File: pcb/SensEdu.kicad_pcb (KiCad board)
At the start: 4 copper layers, 99.1 x 54 mm, 147 parts, among them J1 Power, J10 Barrel_Jack_Switch, J11 Conn_01x04_Pin, J12 Conn_01x04_Pin, J13 Conn_02x01, J14 Conn_02x01, J15 Conn_02x01, J16 Conn_02x01, J19 Conn_03x01, J2 PWM, J20 Conn_01x04_Pin, J3 Analog, J4 PWM, J5 Analog, J6 Communication, J7 Digital, J9 Conn_01x04_Pin, U1 AD8426ACPZ-R7, U12 TLS850C2TE_V33, U13 NCP1117-2.5_SOT223, U2 AD8426ACPZ-R7, U3 LT1790ACS6-1.25, U4 ADA4891, U5 AD8426ACPZ-R7, U6 AD8426ACPZ-R7, U7 ADA4891, U8 DPS310XTSA1

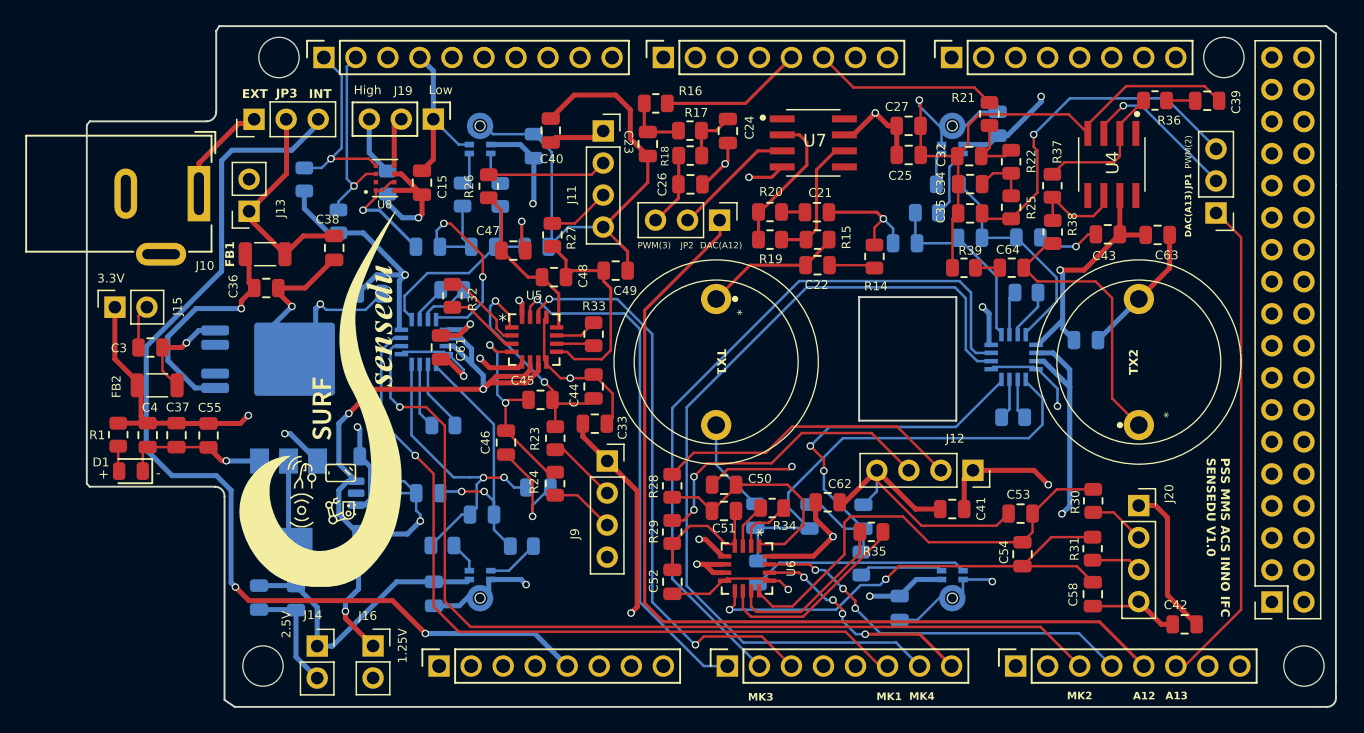
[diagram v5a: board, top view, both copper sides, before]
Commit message: Progress in pcb routing
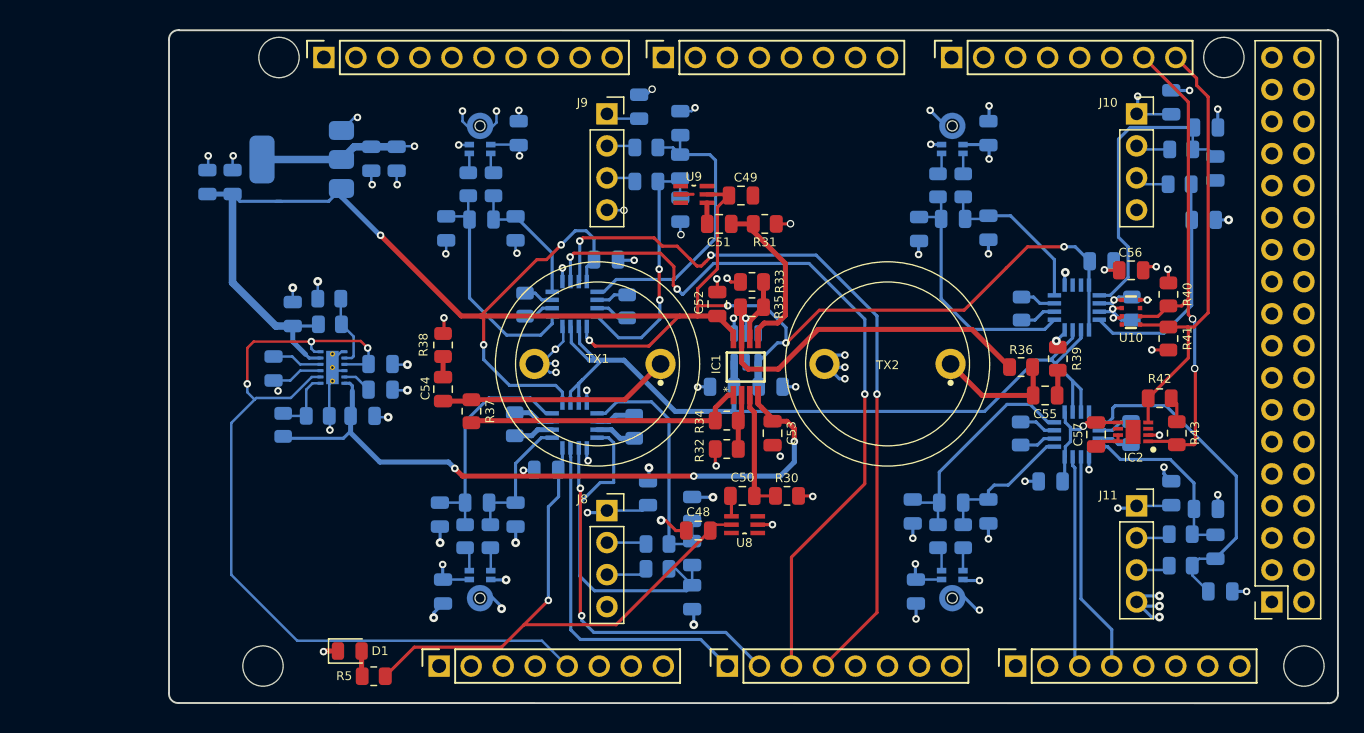
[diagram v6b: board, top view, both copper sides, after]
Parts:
- removed C58: 100p, Capacitor_SMD:C_0805_2012Metric
- removed C61, C62: 1u, Capacitor_SMD:C_0805_2012Metric
- removed C63: 100n, Capacitor_SMD:C_0805_2012Metric
- removed C64: DNI, Capacitor_SMD:C_0805_2012Metric
- removed FB1, FB2: FerriteBead, Inductor_SMD:L_1206_3216Metric
- removed G***: LOGO, wave colour:logo2
- removed the J10 at (108.9, 60.0)
- removed J13, J14, J15, J16: Conn_02x01, Connector_PinSocket_2.54mm:PinSocket_1x02_P2.54mm_Vertical
- removed J19: Conn_03x01, Connector_PinHeader_2.54mm:PinHeader_1x03_P2.54mm_Vertical
- removed JP1, JP2, JP3: Jumper_3_Bridged12, Connector_PinHeader_2.54mm:PinHeader_1x03_P2.54mm_Vertical
- removed LS1, LS2: 328ST16M, SensEdu:328ST16M_Speaker
- removed U12: TLS850C2TE_V33, Package_TO_SOT_SMD:TO-252-4
- removed U13: NCP1117-2.5_SOT223, Package_TO_SOT_SMD:SOT-223-3_TabPin2
- added C19: 100p, Capacitor_SMD:C_0805_2012Metric, B.Cu at (165.5, 85.2)
- added IC1: ADA4511-2ARMZ, SensEdu:ADA4511, F.Cu at (152.2, 73.8)
- added IC2: SHT35-DIS-B2.5KS, SensEdu:SHT35-DIS-B2.5KS, F.Cu at (183.0, 78.9)
- added R43: 10k, Resistor_SMD:R_0805_2012Metric, F.Cu at (186.4, 79.0)
- added TX1: 328ST16M, SensEdu:328ST16M_Speaker, F.Cu at (140.5, 73.5)
- added TX2: 328ST16M, SensEdu:328ST16M_Speaker, F.Cu at (163.5, 73.5)
- added U10: DPS368XTSA1, SensEdu:DPS368XTSA1, F.Cu at (182.8, 69.4)
- added U9: NC7SB3157P6X, SensEdu:SOT65P210X110-6N, F.Cu at (148.1, 60.1)
- C1: value 100n -> 4.7u
- C11: value 100n -> 1u
- C12: value 470p -> 1u
- C13, C17: value 470p -> 100p
- C14: value 1u -> 470p
- C15, C25, C39, C44, C45, C46, R24, R26, R27, R28, R29, U5, U6: moved to B.Cu
- C18: value 100p -> 470p
- C2: value 100n -> 470n
- C20, C7: value 1u -> 100n
- C21, C36: value 100n -> 1u; moved to B.Cu
- C22: value DNI -> 100p; moved to B.Cu
- C23, C35: value 1n -> 100p; moved to B.Cu
- C24, C34: value 1n -> 100n; moved to B.Cu
- C26, C32: value 1n -> 470p; moved to B.Cu
- C27: value 1u -> 470p; moved to B.Cu
- C3: value 10u -> 2.2u; moved to B.Cu
- C31: value 100p -> 1u
- C33, C40, C42: value 100n -> 100p; moved to B.Cu
- C37: value 10u -> 470p; moved to B.Cu
- C38: value 10u -> 100p; moved to B.Cu
- C4: value 100n -> 2.2u; moved to B.Cu
- C41: value 100n -> 470p; moved to B.Cu
- C43: value 1u -> 100n; moved to B.Cu
- C47: value 100p -> 100n; moved to B.Cu
- C48: value 470p -> 10n
- C49: value 100p -> 10n
- C5: value 100p -> 4.7u
- C50: value 100p -> 2.2u
- C51: value 470p -> 2.2u
- C52, C53: value 100p -> 100n
- C54: value 470p -> DNI
- C55: value 100n -> DNI
- C56: value 10u -> 100n; moved to F.Cu
- C57, R42: moved to F.Cu
- C6: value 470p -> 10u
- C9: value 100p -> 10u
- R1: value 47 -> 130k; moved to B.Cu
- R11, R6: value 3.9k -> 1k
- R13, R7: value 1k -> 3.9k
- R14: value DNI -> 3.9k; moved to B.Cu
- R15: value 0 -> 3.9k; moved to B.Cu
- R16, R22: value 4.7k -> 3.9k; moved to B.Cu
- R17, R18, R21, R25: value 4.7k -> 1k; moved to B.Cu
- R19: value 3k -> 3.9k; moved to B.Cu
- R2: value 1k -> 75k
- R20: value 1k -> 3.9k; moved to B.Cu
- R23: value 3.9k -> 1k; moved to B.Cu
- R3: value 3.9k -> 130k
- R30, R31: value 3.9k -> 22k
- R32, R33, R34, R35: value 1k -> 22k
- R36: value 1k -> 0
- R37: value 3k -> 0
- R38: value 0 -> DNI
- R4: value 3.9k -> 75k
- R40, R41: value 10k -> 5k6; moved to F.Cu
- R5: value 3.9k -> 47; moved to F.Cu
- U1: value AD8426ACPZ-R7 -> LM27762DSST; footprint SensEdu:QFN65P400X400X100-16N -> SensEdu:IC_LM27762DSST
- U2: value AD8426ACPZ-R7 -> NCP1117-2.5_SOT223; footprint SensEdu:QFN65P400X400X100-16N -> Package_TO_SOT_SMD:SOT-223-3_TabPin2
- U4, U7: value ADA4891 -> AD8426ACPZ-R7; footprint SensEdu:ADA4891-1ARZ -> SensEdu:QFN65P400X400X100-16N; moved to B.Cu
- U8: value DPS310XTSA1 -> NC7SB3157P6X; footprint SensEdu:XDCR_DPS310XTSA1 -> SensEdu:SOT65P210X110-6N
- moved C56 71.2 mm to (182.8, 66.1), turned to 0 degrees
- moved R40 69.1 mm to (185.8, 68.0)
- moved C57 67.6 mm to (180.0, 79.1), turned to 90 degrees
- moved R41 66.5 mm to (185.8, 71.5), turned to -90 degrees
- moved C55 66.4 mm to (176.0, 76.0), turned to 0 degrees
- moved C36 64.1 mm to (176.4, 82.8), turned to 180 degrees
- moved R42 63.6 mm to (185.1, 76.2), turned to 180 degrees
- moved C6 58.6 mm to (111.6, 59.1), turned to 90 degrees
- moved U2 58.6 mm to (117.0, 57.3), turned to 180 degrees
- moved C46 55.8 mm to (188.8, 85.0), turned to 180 degrees
- moved C47 55.6 mm to (186.0, 83.8), turned to 90 degrees
- moved R26 54.8 mm to (186.7, 59.2), turned to 0 degrees
- moved C45 54.8 mm to (189.5, 88.0), turned to -90 degrees
- moved C2 53.2 mm to (114.8, 73.9)
- moved C1 52.5 mm to (123.3, 73.5), turned to 0 degrees
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- renumbered J3 to J1, J12 to J10, J20 to J11, J5 to J2, J1 to J3, J7 to J4, J2 to J5, J4 to J6, J6 to J7, J9 to J8, J11 to J9, MK4 to MK2, MK2 to MK3, MK3 to MK4
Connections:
- net /48 renamed SE_PWM_3
- C1 pad 1: +2.5V -> /+5V_ARDUINO
- C11 pad 1: +2.5V -> GND
- C11 pad 2: GND -> +1.25V_REF
- C12 pad 1: /Microphones/mic2_out1 -> +3.3V
- C12 pad 2: /Microphones/mic2_out2 -> GND
- C13 pad 1: /Microphones/mic1_out1 -> GND
- C13 pad 2: /Microphones/mic1_out2 -> mic1_out2
- C14 pad 1: +3.3V -> mic1_out1
- C14 pad 2: GND -> mic1_out2
- C15 pad 1: +3.3V -> +2.5V
- C16 pad 2: /Microphones/mic4_out1 -> mic2_out2
- C17 pad 1: /Microphones/mic4_out1 -> GND
- C17 pad 2: /Microphones/mic4_out2 -> mic1_out1
- C18 pad 1: GND -> mic2_out1
- C18 pad 2: /Microphones/mic4_out2 -> mic2_out2
- C2 pad 1: +2.5V -> Net-(U1-C1+)
- C2 pad 2: GND -> Net-(U1-C1-)
- C20 pad 1: +3.3V -> +2.5V
- C21 pad 1: Net-(C21-Pad1) -> +3.3V
- C22 pad 1: Net-(C22-Pad1) -> GND
- C22 pad 2: Net-(C22-Pad2) -> mic4_out2
- C23 pad 1: Net-(C23-Pad1) -> GND
- C23 pad 2: GND -> mic3_out2
- C24 pad 1: Net-(C24-Pad1) -> +2.5V
- C25 pad 1: GND -> +2.5V
- C25 pad 2: +3.3V -> GND
- C26 pad 1: Net-(JP2-B) -> mic3_out1
- C26 pad 2: GND -> mic3_out2
- C27 pad 1: GND -> mic4_out1
- C27 pad 2: +3.3V -> mic4_out2
- C28 pad 2: /Microphones/mic2_out1 -> mic3_out1
- C29 pad 2: /Microphones/mic2_out2 -> mic4_out1
- C3 pad 1: Net-(U12-Q) -> +3.3V
- C30 pad 2: /Microphones/mic1_out1 -> mic5_out2
- C31 pad 1: GND -> +3.3V
- C31 pad 2: /Microphones/mic1_out2 -> GND
- C32 pad 1: Net-(C32-Pad1) -> mic5_out1
- C32 pad 2: GND -> mic5_out2
- C33 pad 1: +2.5V -> GND
- C33 pad 2: GND -> mic5_out1
- C34 pad 1: Net-(C34-Pad1) -> +2.5V
- C35 pad 1: Net-(JP1-B) -> GND
- C35 pad 2: GND -> mic6_out2
- C36 pad 1: Net-(U12-I) -> +3.3V
- C37 pad 1: +3.3V -> mic6_out1
- C37 pad 2: GND -> mic6_out2
- C38 pad 1: Net-(J13-Pin_1) -> GND
- C38 pad 2: GND -> mic6_out1
- C39 pad 1: Net-(C39-Pad1) -> +2.5V
- C4 pad 1: +3.3V -> GND
- C4 pad 2: GND -> -3V3
- C40 pad 1: +2.5V -> GND
- C40 pad 2: GND -> mic7_out2
- C41 pad 1: +2.5V -> mic7_out1
- C41 pad 2: GND -> mic7_out2
- C42 pad 1: +2.5V -> GND
- C42 pad 2: GND -> mic7_out1
- C43 pad 1: GND -> +2.5V
- C43 pad 2: +3.3V -> GND
- C44 pad 2: /Microphones/External Microphone Connectors/mic5_out1 -> mic8_out2
- C45 pad 1: /Microphones/External Microphone Connectors/mic5_out1 -> mic8_out1
- C45 pad 2: /Microphones/External Microphone Connectors/mic5_out2 -> mic8_out2
- C46 pad 2: /Microphones/External Microphone Connectors/mic5_out2 -> mic8_out1
- C47 pad 1: GND -> +2.5V
- C47 pad 2: /Microphones/External Microphone Connectors/mic6_out1 -> GND
- C48 pad 1: /Microphones/External Microphone Connectors/mic6_out1 -> GND
- C48 pad 2: /Microphones/External Microphone Connectors/mic6_out2 -> +3.3V
- C49 pad 2: /Microphones/External Microphone Connectors/mic6_out2 -> +3.3V
- C5 pad 1: GND -> /Power/CP
- C5 pad 2: /Microphones/mic3_out1 -> GND
- C50 pad 1: GND -> /Speakers/SW1_OUT
- C50 pad 2: /Microphones/External Microphone Connectors/mic7_out1 -> /Speakers/+IN_CH1
- C51 pad 1: /Microphones/External Microphone Connectors/mic7_out1 -> /Speakers/SW2_OUT
- C51 pad 2: /Microphones/External Microphone Connectors/mic7_out2 -> /Speakers/+IN_CH2
- C52 pad 1: GND -> +3.3V
- C52 pad 2: /Microphones/External Microphone Connectors/mic7_out2 -> GND
- C53 pad 2: /Microphones/External Microphone Connectors/mic8_out1 -> -3V3
- C54 pad 1: /Microphones/External Microphone Connectors/mic8_out1 -> /Speakers/TX1
- C54 pad 2: /Microphones/External Microphone Connectors/mic8_out2 -> Net-(C54-Pad2)
- C55 pad 1: +3.3V -> /Speakers/TX2
- C55 pad 2: GND -> Net-(C55-Pad2)
- C57 pad 1: +2.5V -> GND
- C57 pad 2: GND -> +3.3V
- C6 pad 1: /Microphones/mic3_out1 -> +3.3V
- C6 pad 2: /Microphones/mic3_out2 -> GND
- C7 pad 1: GND -> +3.3V
- C7 pad 2: +1.25V_REF -> GND
- C9 pad 1: GND -> +2.5V
- C9 pad 2: /Microphones/mic3_out2 -> GND
- D1 pad 2: Net-(D1-A) -> /Power/LED+
- J1 pad 1: /A0 -> /OUT_MIC5
- J1 pad 2: /A1 -> /OUT_MIC6
- J1 pad 3: /A2 -> /OUT_MIC2
- J1 pad 4: /A3 -> /OUT_MIC1
- J1 pad 6: /A5 -> unconnected-(J1-Pin_6-Pad6)
- J1 pad 7: /A6 -> unconnected-(J1-Pin_7-Pad7)
- J1 pad 8: /A7 -> unconnected-(J1-Pin_8-Pad8)
- J10 pad 2: Net-(J12-Pin_2) -> /Microphones/External Microphone Connectors/out+
- J10 pad 3: Net-(J12-Pin_3) -> /Microphones/External Microphone Connectors/out-
- J11 pad 2: Net-(J20-Pin_2) -> /Microphones/External Microphone Connectors/out+
- J11 pad 3: Net-(J20-Pin_3) -> /Microphones/External Microphone Connectors/out-
- J2 pad 1: /A8 -> /OUT_MIC3
- J2 pad 2: /A9 -> /OUT_MIC4
- J2 pad 3: /A10 -> /OUT_MIC7
- J2 pad 4: /Microphones/MIC7_OUT -> /OUT_MIC8
- J2 pad 5: A12 -> DAC0
- J2 pad 6: A13 -> DAC1
- J3 pad 5: /5V0 -> /+5V_ARDUINO
- J4 pad 20: /37 -> SE_PWM_2
- J6 pad 1: /*7 -> S1
- J6 pad 2: /*6 -> S2
- J6 pad 4: /*4 -> SE_PWM_1
- J6 pad 5: /*3 -> /4*
- J6 pad 6: /*2 -> /3*
- J7 pad 7: /SDA/20 -> /SDA
- J7 pad 8: /SCL/21 -> /SCL
- J8 pad 2: Net-(J9-Pin_2) -> /Microphones/External Microphone Connectors/out+
- J8 pad 3: Net-(J9-Pin_3) -> /Microphones/External Microphone Connectors/out-
- J9 pad 2: Net-(J11-Pin_2) -> /Microphones/External Microphone Connectors/out+
- J9 pad 3: Net-(J11-Pin_3) -> /Microphones/External Microphone Connectors/out-
- MK2 pad 3: Net-(MK4-OUTPUT-) -> Net-(MK2-OUTPUT-)
- MK3 pad 1: Net-(MK2-OUTPUT+) (its old number) -> Net-(MK3-OUTPUT+)
- MK3 pad 3: Net-(MK2-OUTPUT-) -> Net-(MK3-OUTPUT-)
- MK4 pad 1: Net-(MK3-OUTPUT+) -> Net-(MK4-OUTPUT+)
- MK4 pad 3: Net-(MK3-OUTPUT-) -> Net-(MK4-OUTPUT-)
- R1 pad 2: Net-(D1-A) -> /Power/FB+
- R10 pad 2: /Microphones/mic4_out1 -> mic2_out1
- R11 pad 1: Net-(MK4-OUTPUT-) -> Net-(U4-RG2_2)
- R11 pad 2: /Microphones/mic4_out2 -> Net-(U4-RG2)
- R12 pad 1: Net-(U2-RG1_2) -> Net-(U5-RG1_2)
- R12 pad 2: Net-(U2-RG1) -> Net-(U5-RG1)
- R13 pad 1: Net-(U2-RG2_2) -> Net-(MK4-OUTPUT-)
- R13 pad 2: Net-(U2-RG2) -> mic4_out2
- R14 pad 1: GND -> Net-(MK3-OUTPUT-)
- R14 pad 2: Net-(C22-Pad2) -> mic3_out2
- R15 pad 1: Net-(U7-OUT) -> Net-(MK3-OUTPUT+)
- R15 pad 2: Net-(C22-Pad1) -> mic3_out1
- R16 pad 1: Net-(C23-Pad1) -> Net-(MK4-OUTPUT+)
- R16 pad 2: /*3 -> mic4_out1
- R17 pad 1: Net-(C23-Pad1) -> Net-(U5-RG2_2)
- R17 pad 2: Net-(C24-Pad1) -> Net-(U5-RG2)
- R18 pad 1: Net-(C24-Pad1) -> Net-(U6-RG1_2)
- R18 pad 2: Net-(JP2-B) -> Net-(U6-RG1)
- R19 pad 1: Net-(U7--IN) -> /Microphones/External Microphone Connectors/out-
- R19 pad 2: Net-(U7-OUT) -> mic5_out2
- R2 pad 1: Net-(U1-RG1_2) -> /Power/FB+
- R2 pad 2: Net-(U1-RG1) -> GND
- R20 pad 1: Net-(U7--IN) -> /Microphones/External Microphone Connectors/out+
- R20 pad 2: Net-(C21-Pad1) -> mic5_out1
- R21 pad 1: Net-(C32-Pad1) -> Net-(U6-RG2_2)
- R21 pad 2: /*2 -> Net-(U6-RG2)
- R22 pad 1: Net-(C32-Pad1) -> /Microphones/External Microphone Connectors/out-
- R22 pad 2: Net-(C34-Pad1) -> mic6_out2
- R23 pad 1: Net-(J9-Pin_2) -> Net-(U7-RG1_2)
- R23 pad 2: /Microphones/External Microphone Connectors/mic5_out1 -> Net-(U7-RG1)
- R24 pad 1: Net-(J9-Pin_3) -> /Microphones/External Microphone Connectors/out+
- R24 pad 2: /Microphones/External Microphone Connectors/mic5_out2 -> mic6_out1
- R25 pad 1: Net-(C34-Pad1) -> Net-(U7-RG2_2)
- R25 pad 2: Net-(JP1-B) -> Net-(U7-RG2)
- R26 pad 1: Net-(J11-Pin_2) -> /Microphones/External Microphone Connectors/out-
- R26 pad 2: /Microphones/External Microphone Connectors/mic6_out1 -> mic7_out2
- R27 pad 1: Net-(J11-Pin_3) -> /Microphones/External Microphone Connectors/out+
- R27 pad 2: /Microphones/External Microphone Connectors/mic6_out2 -> mic7_out1
- R28 pad 1: Net-(J12-Pin_2) -> /Microphones/External Microphone Connectors/out-
- R28 pad 2: /Microphones/External Microphone Connectors/mic7_out1 -> mic8_out2
- R29 pad 1: Net-(J12-Pin_3) -> /Microphones/External Microphone Connectors/out+
- R29 pad 2: /Microphones/External Microphone Connectors/mic7_out2 -> mic8_out1
- R3 pad 1: Net-(MK2-OUTPUT+) (its old number) -> GND
- R3 pad 2: /Microphones/mic2_out1 -> /Power/FB-
- R30 pad 1: Net-(J20-Pin_2) -> GND
- R30 pad 2: /Microphones/External Microphone Connectors/mic8_out1 -> /Speakers/+IN_CH1
- R31 pad 1: Net-(J20-Pin_3) -> GND
- R31 pad 2: /Microphones/External Microphone Connectors/mic8_out2 -> /Speakers/+IN_CH2
- R32 pad 1: Net-(U5-RG1_2) -> GND
- R32 pad 2: Net-(U5-RG1) -> /Speakers/-IN_CH1
- R33 pad 1: Net-(U5-RG2_2) -> GND
- R33 pad 2: Net-(U5-RG2) -> /Speakers/-IN_CH2
- R34 pad 1: Net-(U6-RG1_2) -> /Speakers/-IN_CH1
- R34 pad 2: Net-(U6-RG1) -> /Speakers/TX1_IN
- R35 pad 1: Net-(U6-RG2_2) -> /Speakers/-IN_CH2
- R35 pad 2: Net-(U6-RG2) -> /Speakers/TX2_IN
- R36 pad 1: Net-(U4--IN) -> /Speakers/TX2_IN
- R36 pad 2: Net-(C39-Pad1) -> /Speakers/TX2
- R37 pad 1: Net-(U4--IN) -> /Speakers/TX1_IN
- R37 pad 2: Net-(U4-OUT) -> /Speakers/TX1
- R38 pad 1: Net-(U4-OUT) -> GND
- R38 pad 2: Net-(C64-Pad1) -> Net-(C54-Pad2)
- R39 pad 2: Net-(C64-Pad2) -> Net-(C55-Pad2)
- R4 pad 1: Net-(MK1-OUTPUT+) -> /Power/FB-
- R4 pad 2: /Microphones/mic1_out1 -> -3V3
- R40 pad 1: /SCL1 -> +2.5V
- R40 pad 2: +3.3V -> /SDA
- R41 pad 1: +3.3V -> /SCL
- R41 pad 2: /SDA1 -> +2.5V
- R42 pad 1: Net-(J19-B) -> +3.3V
- R42 pad 2: +3.3V -> /SCL
- R5 pad 1: Net-(MK1-OUTPUT-) -> +3.3V
- R5 pad 2: /Microphones/mic1_out2 -> /Power/LED+
- R6 pad 1: Net-(MK2-OUTPUT-) -> Net-(U4-RG1_2)
- R6 pad 2: /Microphones/mic2_out2 -> Net-(U4-RG1)
- R7 pad 1: Net-(U1-RG2_2) -> Net-(MK1-OUTPUT-)
- R7 pad 2: Net-(U1-RG2) -> mic1_out2
- R8 pad 1: Net-(MK3-OUTPUT+) -> Net-(MK2-OUTPUT-)
- R8 pad 2: /Microphones/mic3_out1 -> mic2_out2
- R9 pad 1: Net-(MK3-OUTPUT-) -> Net-(MK1-OUTPUT+)
- R9 pad 2: /Microphones/mic3_out2 -> mic1_out1
- U1 pad 1: /Microphones/mic1_out1 -> GND
- U1 pad 10: Net-(U1-RG2_2) -> Net-(U1-C1+)
- U1 pad 11: Net-(U1-RG2) -> +3.3V
- U1 pad 12: /Microphones/mic2_out1 -> /+5V_ARDUINO
- U1 pad 14: /A10 -> GND
- U1 pad 15: /A5 -> GND
- U1 pad 16: +3.3V -> GND
- U1 pad 2: Net-(U1-RG1_2) -> /Power/FB+
- U1 pad 3: Net-(U1-RG1) -> /+5V_ARDUINO
- U1 pad 4: /Microphones/mic1_out2 -> GND
- U1 pad 5: +3.3V -> /Power/CP
- U1 pad 6: +1.25V_REF -> -3V3
- U1 pad 7: +1.25V_REF -> /Power/FB-
- U1 pad 8: GND -> /+5V_ARDUINO
- U1 pad 9: /Microphones/mic2_out2 -> Net-(U1-C1-)
- U2 pad 1: /Microphones/mic3_out1 -> GND
- U2 pad 2: Net-(U2-RG1_2) -> +2.5V
- U2 pad 3: Net-(U2-RG1) -> +3.3V
- U4 pad 1: unconnected-(U4-NC_1-Pad1) -> mic6_out1
- U4 pad 2: Net-(U4--IN) -> Net-(U4-RG1_2)
- U4 pad 3: Net-(JP1-C) -> Net-(U4-RG1)
- U4 pad 4: GND -> mic6_out2
- U4 pad 5: unconnected-(U4-NC_2-Pad5) -> +3.3V
- U4 pad 6: Net-(U4-OUT) -> +1.25V_REF
- U4 pad 7: +3.3V -> +1.25V_REF
- U4 pad 8: unconnected-(U4-NC_3-Pad8) -> GND
- U5 pad 1: /Microphones/External Microphone Connectors/mic5_out1 -> mic7_out1
- U5 pad 12: /Microphones/External Microphone Connectors/mic6_out1 -> mic4_out1
- U5 pad 14: /A2 -> /OUT_MIC4
- U5 pad 15: /A0 -> /OUT_MIC3
- U5 pad 4: /Microphones/External Microphone Connectors/mic5_out2 -> mic7_out2
- U5 pad 9: /Microphones/External Microphone Connectors/mic6_out2 -> mic4_out2
- U6 pad 1: /Microphones/External Microphone Connectors/mic7_out1 -> mic3_out2
- U6 pad 12: /Microphones/External Microphone Connectors/mic8_out1 -> mic5_out2
- U6 pad 14: /A7 -> /OUT_MIC6
- U6 pad 15: /Microphones/MIC7_OUT -> /OUT_MIC5
- U6 pad 4: /Microphones/External Microphone Connectors/mic7_out2 -> mic3_out1
- U6 pad 9: /Microphones/External Microphone Connectors/mic8_out2 -> mic5_out1
- U7 pad 1: unconnected-(U7-NC_1-Pad1) -> mic2_out2
- U7 pad 2: Net-(U7--IN) -> Net-(U7-RG1_2)
- U7 pad 3: Net-(JP2-C) -> Net-(U7-RG1)
- U7 pad 4: GND -> mic2_out1
- U7 pad 5: unconnected-(U7-NC_2-Pad5) -> +3.3V
- U7 pad 6: Net-(U7-OUT) -> +1.25V_REF
- U7 pad 7: +3.3V -> +1.25V_REF
- U7 pad 8: unconnected-(U7-NC_3-Pad8) -> GND
- U8 pad 1: GND -> SE_PWM_1
- U8 pad 2: unconnected-(U8-~{CSB}-Pad2) -> GND
- U8 pad 3: /SDA1 -> DAC0
- U8 pad 4: /SCL1 -> /Speakers/SW1_OUT
- U8 pad 5: Net-(J19-C) -> +3.3V
- U8 pad 6: +3.3V -> S1
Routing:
- net GND: track 320.6 -> 116.6 mm, vias 19 -> 82
- net +2.5V: track 190.7 -> 46.6 mm, vias 5 -> 13
- net /5V0: track 79.1 -> 0.00 mm, vias 2 -> 0
- net /A10: track 76.3 -> 0.00 mm, vias 1 -> 0
- net A12: track 74.4 -> 0.00 mm
- net /+5V_ARDUINO: track 0.00 -> 69.2 mm, vias 0 -> 3
- net /A6: track 68.0 -> 0.00 mm
- net +1.25V_REF: track 134.0 -> 71.4 mm, vias 5 -> 0
- net /A5: track 61.8 -> 0.00 mm, vias 1 -> 0
- net /OUT_MIC2: track 0.00 -> 60.5 mm, vias 0 -> 3
- net /OUT_MIC1: track 0.00 -> 59.8 mm, vias 0 -> 3
- net /A1: track 57.6 -> 0.00 mm
- net -3V3: track 0.00 -> 54.0 mm, vias 0 -> 3
- net /A2: track 45.9 -> 0.00 mm, vias 2 -> 0
- net /A0: track 41.3 -> 0.00 mm, vias 1 -> 0
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- removed copper zone on In2.Cu, net +3.3V
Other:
- board size 99.1 x 54 mm -> 92.7 x 53.4 mm
- board text added: "10.39394 mm is the wavelength of 33khz sound wave in air at 20 degrees nlambda/2 is the spacing"
- board text removed: "A12"
- board text removed: "A13"
- board text removed: "DAC(A12)"
- board text removed: "DAC(A13)"
- board text removed: "EXT"
- board text removed: "INT"
- board text removed: "MK1"
- board text removed: "MK2"
- board text removed: "MK3"
- board text removed: "MK4"
- board text removed: "PSS MMS ACS INNO IFC SENSEDU V1.0"
- board text removed: "PWM(2)"
- board text removed: "PWM(3)"

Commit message: pcb routing finished
very messy
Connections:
- J10 pad 2: /Microphones/External Microphone Connectors/out+ -> Net-(J10-Pin_2)
- J10 pad 3: /Microphones/External Microphone Connectors/out- -> Net-(J10-Pin_3)
- J8 pad 2: /Microphones/External Microphone Connectors/out+ -> Net-(J8-Pin_2)
- J8 pad 3: /Microphones/External Microphone Connectors/out- -> Net-(J8-Pin_3)
- J9 pad 2: /Microphones/External Microphone Connectors/out+ -> Net-(J9-Pin_2)
- J9 pad 3: /Microphones/External Microphone Connectors/out- -> Net-(J9-Pin_3)
- R19 pad 1: /Microphones/External Microphone Connectors/out- -> Net-(J8-Pin_3)
- R20 pad 1: /Microphones/External Microphone Connectors/out+ -> Net-(J8-Pin_2)
- R22 pad 1: /Microphones/External Microphone Connectors/out- -> Net-(J9-Pin_3)
- R24 pad 1: /Microphones/External Microphone Connectors/out+ -> Net-(J9-Pin_2)
- R26 pad 1: /Microphones/External Microphone Connectors/out- -> Net-(J10-Pin_3)
- R27 pad 1: /Microphones/External Microphone Connectors/out+ -> Net-(J10-Pin_2)
- U8 pad 1: SE_PWM_1 -> SE_PWM_3
- U9 pad 1: SE_PWM_2 -> SE_PWM_1
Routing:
- net DAC1: track 0.00 -> 85.3 mm, vias 0 -> 9
- net S1: track 0.00 -> 61.7 mm, vias 0 -> 3
- net /OUT_MIC3: track 0.00 -> 51.6 mm, vias 0 -> 5
- net /OUT_MIC4: track 0.00 -> 49.3 mm, vias 0 -> 5
- net +3.3V: track 224.0 -> 269.6 mm, vias 9 -> 12
- net SE_PWM_3: track 0.00 -> 43.8 mm, vias 0 -> 4
- net DAC0: track 0.00 -> 36.4 mm, vias 0 -> 2
- net SE_PWM_1: track 0.00 -> 13.9 mm, vias 0 -> 2
- net S2: track 0.00 -> 10.6 mm
- net /Microphones/External Microphone Connectors/out-: track 11.0 -> 2.73 mm
- net /Microphones/External Microphone Connectors/out+: track 10.9 -> 2.71 mm
- net Net-(J8-Pin_3): track 0.00 -> 3.28 mm
- net Net-(J8-Pin_2): track 0.00 -> 3.14 mm
- net Net-(J10-Pin_2): track 0.00 -> 2.74 mm
- net Net-(J10-Pin_3): track 0.00 -> 2.71 mm
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
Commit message: pcb layout polishing
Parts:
- added G***: LOGO, SensEdu:logo2, F.Cu at (114.3, 71.3)
- added TP_1V25: TestPoint, TestPoint:TestPoint_THTPad_D2.0mm_Drill1.0mm, F.Cu at (159.7, 85.3)
- added TP_2V5: TestPoint, TestPoint:TestPoint_THTPad_D2.0mm_Drill1.0mm, F.Cu at (109.7, 53.1)
- added TP_3V3: TestPoint, TestPoint:TestPoint_THTPad_D2.0mm_Drill1.0mm, F.Cu at (109.3, 66.6)
- added TP_NEG_3V3: TestPoint, TestPoint:TestPoint_THTPad_D2.0mm_Drill1.0mm, F.Cu at (121.2, 83.8)
- moved C42 0.29 mm to (188.8, 54.5)
- renumbered MK2 to MIC2, MK3 to MIC3, MK4 to MIC4, U9 to SW2
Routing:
- net +1.25V_REF: track 71.4 -> 80.2 mm
- net +2.5V: track 46.6 -> 55.5 mm, vias 13 -> 11
- net +3.3V: track 269.6 -> 277.4 mm, vias 12 -> 13
- net mic8_out1: track 14.7 -> 22.3 mm
- net -3V3: track 54.0 -> 58.3 mm
- net mic8_out2: track 26.1 -> 30.0 mm
- net /+5V_ARDUINO: track 69.2 -> 68.0 mm
- net GND: track 117.7 -> 116.6 mm, vias 84 -> 86
- net DAC1: track 85.3 -> 86.3 mm
- net /SDA: track 40.6 -> 39.7 mm
- net Net-(J10-Pin_3): track 2.71 -> 2.00 mm
- net mic4_out2: track 20.3 -> 19.7 mm
- net mic4_out1: track 13.3 -> 12.7 mm
- net mic7_out1: track 24.3 -> 23.8 mm
- net /OUT_MIC7: track 16.8 -> 16.3 mm
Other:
- board text added: "+"
- board text added: "-"
- board text added: "2.5V"
- board text added: "3.3V -> 2.5V"
- board text added: "3.3V->1.25V"
- board text added: "5V"
- board text added: "5V -> +/-3.3V"
- board text added: "AMP1"
- board text added: "AMP2"
- board text added: "AMP3"
- board text added: "AMP4"
- board text added: "DAC0"
- board text added: "DAC1"
- board text added: "GND"
- board text added: "MIC1"
- board text added: "MIC2"
- board text added: "MIC3"
- board text added: "MIC4"
- board text added: "PREAMP1"
- board text added: "PREAMP2"
- board text added: "PREAMP3"
- board text added: "PREAMP4"
- board text added: "PWR"
- board text added: "S1"
- board text added: "S2"
- board text added: "SCL"
- board text added: "SDA"
